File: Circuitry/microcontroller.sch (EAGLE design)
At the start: 8 parts

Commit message: fix the microcontroller board
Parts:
- removed SPACER: (no value), pinhead:PINHD-1X10
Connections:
- net N$1: now also TRANSISTOR.3; no longer LED.1
- net N$2: now also LED.1; no longer TRANSISTOR.3
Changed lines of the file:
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@@
 <part name="ESP1-15" library="pinhead" library_urn="urn:adsk.eagle:library:325" deviceset="PINHD-1X15" device="" package3d_urn="urn:adsk.eagle:package:22424/2"/>
 <part name="ESP16-30" library="pinhead" library_urn="urn:adsk.eagle:library:325" deviceset="PINHD-1X15" device="" package3d_urn="urn:adsk.eagle:package:22424/2"/>
-<part name="SPACER" library="pinhead" library_urn="urn:adsk.eagle:library:325" deviceset="PINHD-1X10" device="" package3d_urn="urn:adsk.eagle:package:22406/2"/>
 <part name="R1" library="rcl" library_urn="urn:adsk.eagle:library:334" deviceset="R-US_" device="0207/7" package3d_urn="urn:adsk.eagle:package:23493/2"/>
 </parts>
@@
 <attribute name="VALUE" x="33.02" y="44.45" size="1.778" layer="96" rot="R270"/>
 </instance>
-<instance part="SPACER" gate="A" x="106.68" y="60.96" smashed="yes">
-<attribute name="NAME" x="100.33" y="74.295" size="1.778" layer="95"/>
-<attribute name="VALUE" x="100.33" y="43.18" size="1.778" layer="96"/>
-</instance>
 <instance part="R1" gate="G$1" x="55.88" y="60.96" smashed="yes" rot="R90">
 <attribute name="NAME" x="54.3814" y="57.15" size="1.778" layer="95" rot="R90"/>
@@
 <net name="N$1" class="0">
 <segment>
-<pinref part="LED" gate="G$1" pin="1"/>
-<wire x1="12.7" y1="60.96" x2="12.7" y2="83.82" width="0.1524" layer="91"/>
-<wire x1="12.7" y1="83.82" x2="71.12" y2="83.82" width="0.1524" layer="91"/>
 <pinref part="SWITCH" gate="G$1" pin="1"/>
 <wire x1="71.12" y1="83.82" x2="78.74" y2="83.82" width="0.1524" layer="91"/>
@@
 <pinref part="ESP1-15" gate="A" pin="14"/>
 <wire x1="71.12" y1="71.12" x2="71.12" y2="83.82" width="0.1524" layer="91"/>
-<junction x="71.12" y="83.82"/>
+<pinref part="TRANSISTOR" gate="A" pin="3"/>
+<wire x1="58.42" y1="50.8" x2="58.42" y2="58.42" width="0.1524" layer="91"/>
+<wire x1="58.42" y1="58.42" x2="71.12" y2="58.42" width="0.1524" layer="91"/>
+<wire x1="71.12" y1="58.42" x2="71.12" y2="71.12" width="0.1524" layer="91"/>
+<junction x="71.12" y="71.12"/>
 </segment>
 </net>
@@
 <segment>
 <pinref part="ESP1-15" gate="A" pin="15"/>
-<wire x1="73.66" y1="71.12" x2="73.66" y2="60.96" width="0.1524" layer="91"/>
-<pinref part="TRANSISTOR" gate="A" pin="3"/>
-<wire x1="73.66" y1="60.96" x2="58.42" y2="60.96" width="0.1524" layer="91"/>
-<wire x1="58.42" y1="60.96" x2="58.42" y2="50.8" width="0.1524" layer="91"/>
 <pinref part="BOOSTCONVERTER" gate="G$1" pin="2"/>
-<wire x1="73.66" y1="60.96" x2="73.66" y2="48.26" width="0.1524" layer="91"/>
+<wire x1="73.66" y1="71.12" x2="73.66" y2="48.26" width="0.1524" layer="91"/>
 <wire x1="73.66" y1="48.26" x2="86.36" y2="48.26" width="0.1524" layer="91"/>
-<junction x="73.66" y="60.96"/>
+<pinref part="LED" gate="G$1" pin="1"/>
+<wire x1="12.7" y1="60.96" x2="12.7" y2="78.74" width="0.1524" layer="91"/>
+<wire x1="12.7" y1="78.74" x2="73.66" y2="78.74" width="0.1524" layer="91"/>
+<wire x1="73.66" y1="78.74" x2="73.66" y2="71.12" width="0.1524" layer="91"/>
+<junction x="73.66" y="71.12"/>
 </segment>
 </net>

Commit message: add initial components and header pins to board
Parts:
- removed BOOSTCONVERTER, LED, SWITCH: (no value), pinhead:PINHD-1X2
- removed ESP1-15, ESP16-30: (no value), pinhead:PINHD-1X15
- removed R1: (no value), rcl:R-US_0207/7
- removed TRANSISTOR: (no value), pinhead:PINHD-1X3
- added BAT_READ, TRIGGER: (no value), pinhead:PINHD-1X1
- added IR_LED, OLED, PWR: (no value), pinhead:PINHD-1X2
- added IR_TRS: 2N5088, transistor-npn:2N5088
- added JP3, JP4: (no value), pinhead:PINHD-1X15
- added LED_CTRL: (no value), pinhead:PINHD-1X4
- added SHIFT_REG: (no value), pinhead:PINHD-1X5
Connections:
- removed net N$2: BOOSTCONVERTER.2, ESP1-15.15, LED.1
- removed net N$3: R1.1, TRANSISTOR.2
- removed net N$4: ESP16-30.14, R1.2
- removed net N$5: ESP16-30.13, SWITCH.2
- removed net N$6: LED.2, TRANSISTOR.1
- new net 0: IR_LED.2, JP3.14, LED_CTRL.4, PWR.2, SHIFT_REG.5
- new net BATTERY_CHECKER: BAT_READ.1, JP3.1
- new net B_CTRL: JP4.13, LED_CTRL.3
- new net CLOCK: JP4.8, SHIFT_REG.3
- new net DATA: JP4.5, SHIFT_REG.2
- new net G_CTRL: JP4.11, LED_CTRL.2
- new net IR_LED: IR_TRS.B, JP4.4
- new net LATCH: JP4.9, SHIFT_REG.4
- new net OLED_SCL_PIN: JP4.2, OLED.1
- new net OLED_SDA: JP4.3, OLED.2
- new net R_CTRL: JP4.10, LED_CTRL.1
- new net TRIGGER: JP4.1, TRIGGER.1
- new net VCC: IR_TRS.C, JP3.15, PWR.1, SHIFT_REG.1
- net N$1: now also IR_LED.1, IR_TRS.E; no longer BOOSTCONVERTER.1, ESP1-15.14, SWITCH.1, TRANSISTOR.3
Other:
- note added: "A0 - GPIO 16"
- note added: "ESP Top View"
- note added: "Vin ----- 3.3 V"

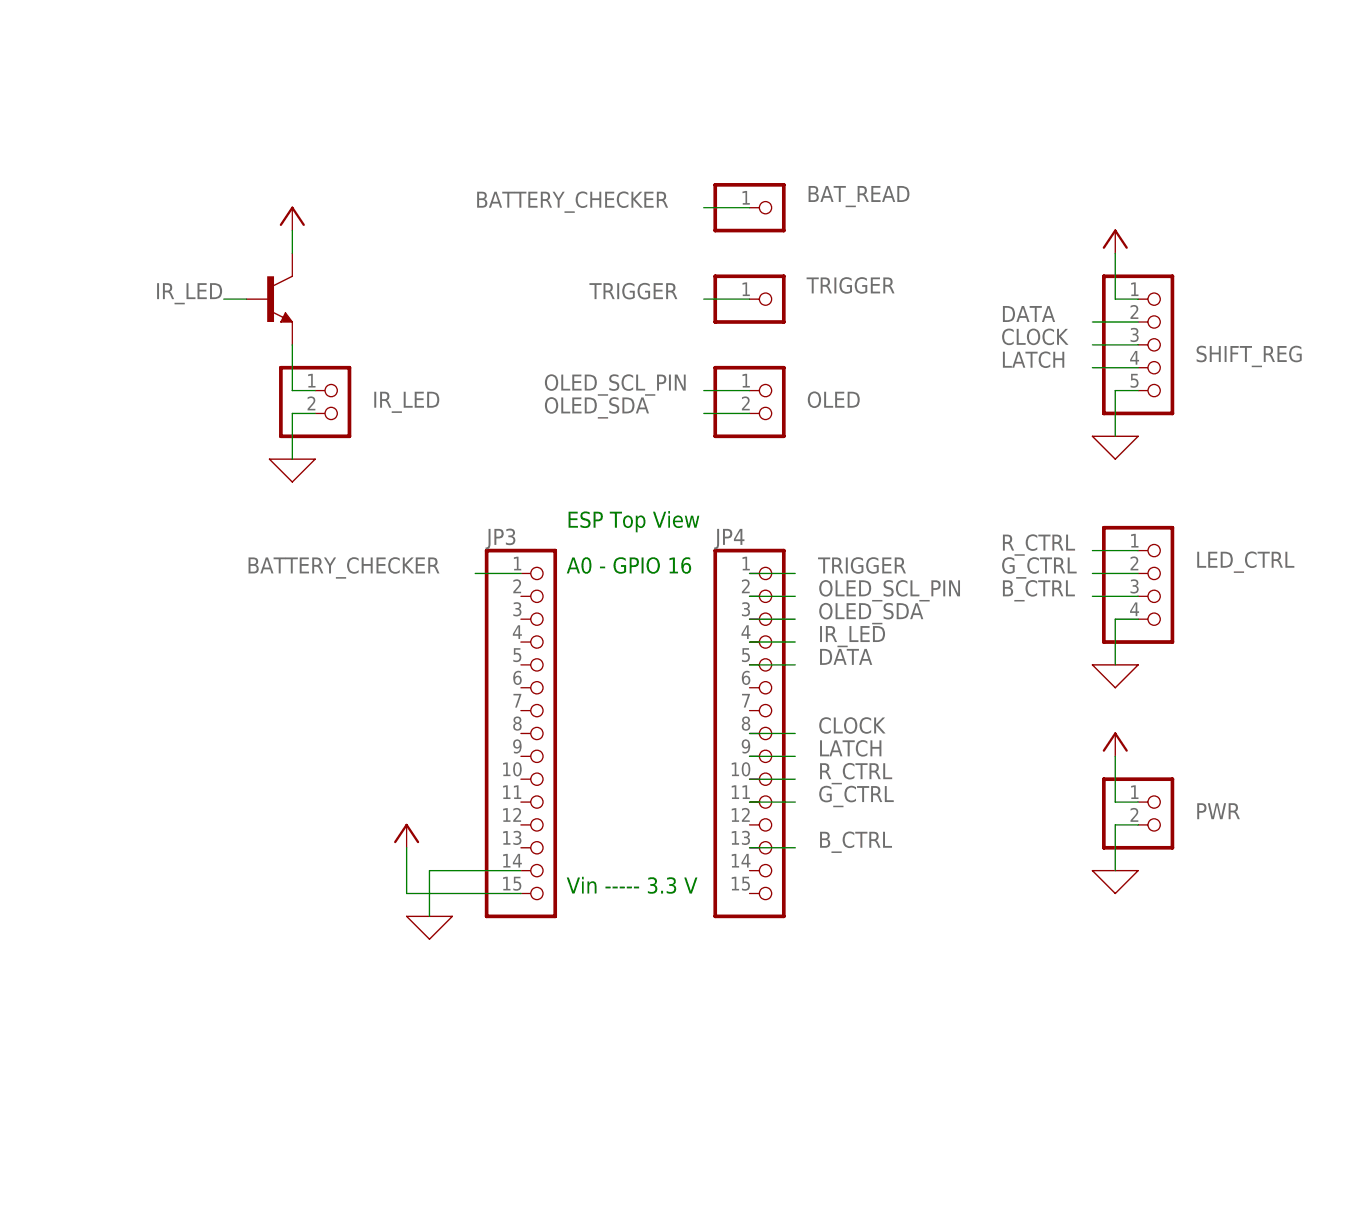
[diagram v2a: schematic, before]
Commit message: create microcontroller board
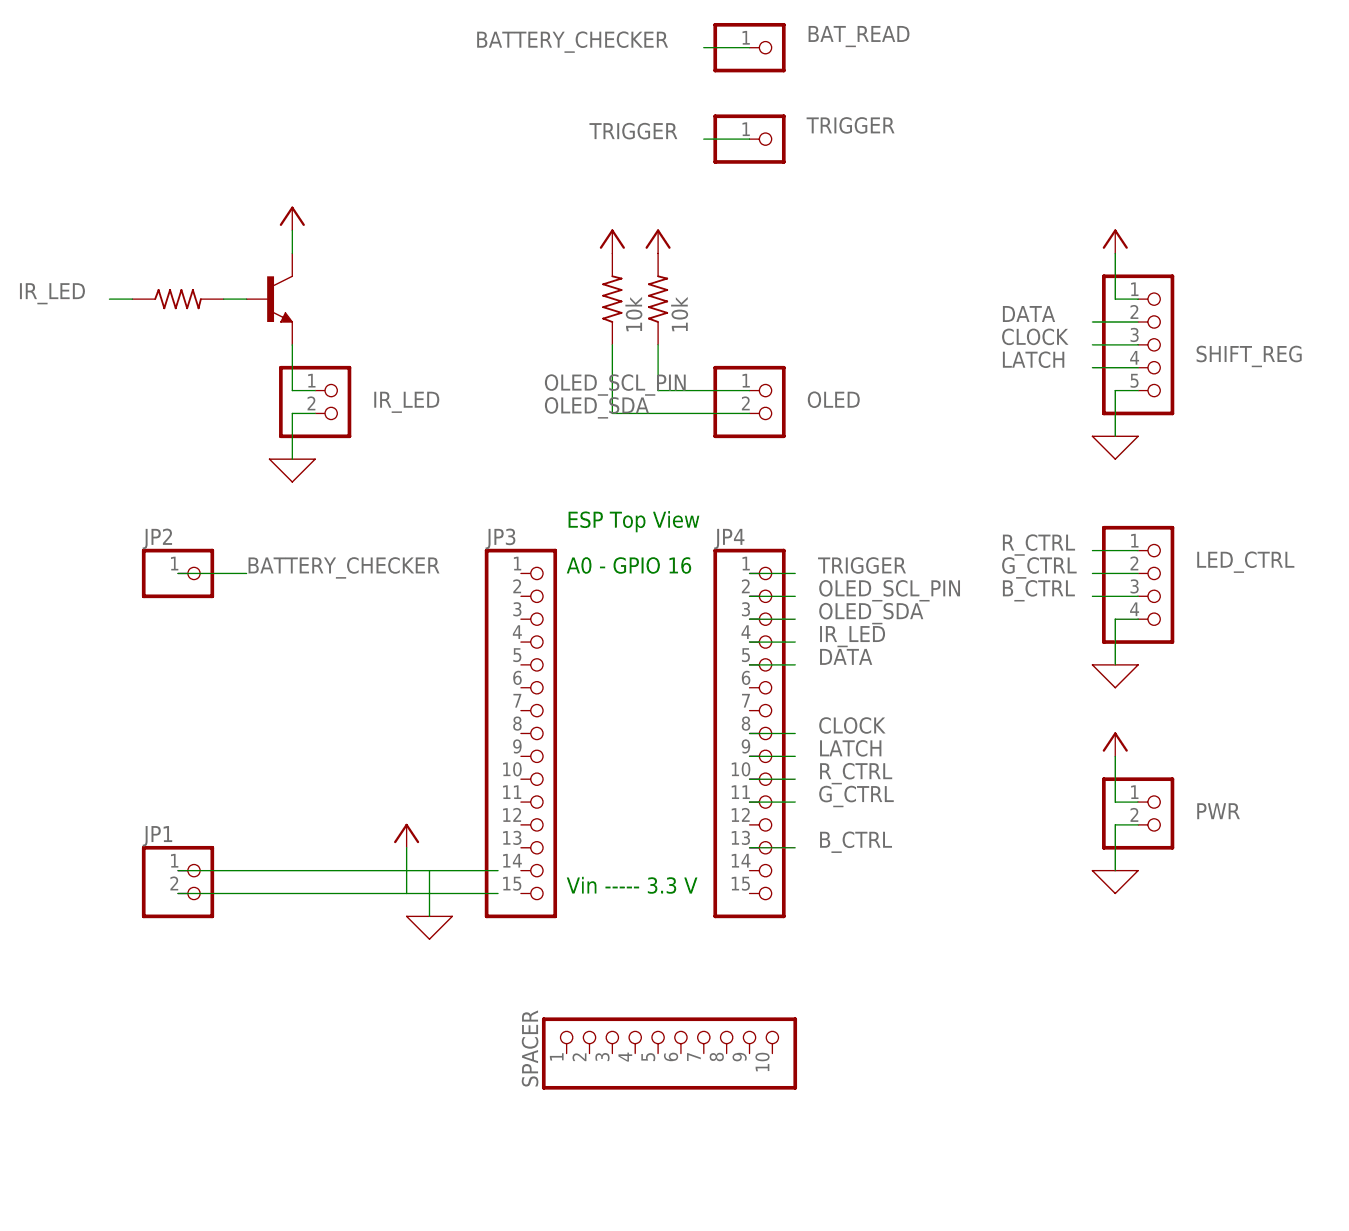
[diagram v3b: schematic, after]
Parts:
- added JP1: (no value), pinhead:PINHD-1X2
- added JP2: (no value), pinhead:PINHD-1X1
- added R1, R2: 10k, rcl:R-US_0204/7
- added R3: (no value), rcl:R-US_0204/7
- added SPACER: (no value), pinhead:PINHD-1X10
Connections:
- new net N$2: IR_TRS.B, R3.2
- net 0: now also JP1.1; no longer JP3.14
- net BATTERY_CHECKER: now also JP2.1; no longer JP3.1
- net IR_LED: now also R3.1; no longer IR_TRS.B
- net OLED_SCL_PIN: now also R1.1
- net OLED_SDA: now also R2.1
- net VCC: now also JP1.2, R1.2, R2.2; no longer JP3.15
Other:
- moved on the sheet: BAT_READ, TRIGGER

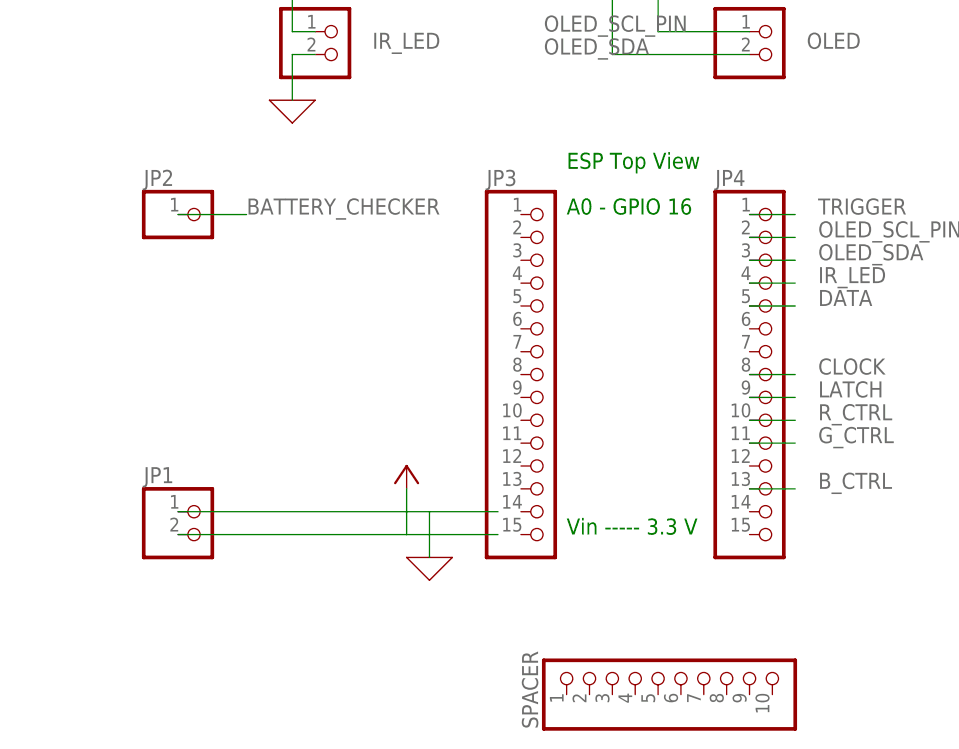
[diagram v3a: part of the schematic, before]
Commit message: remove header pins
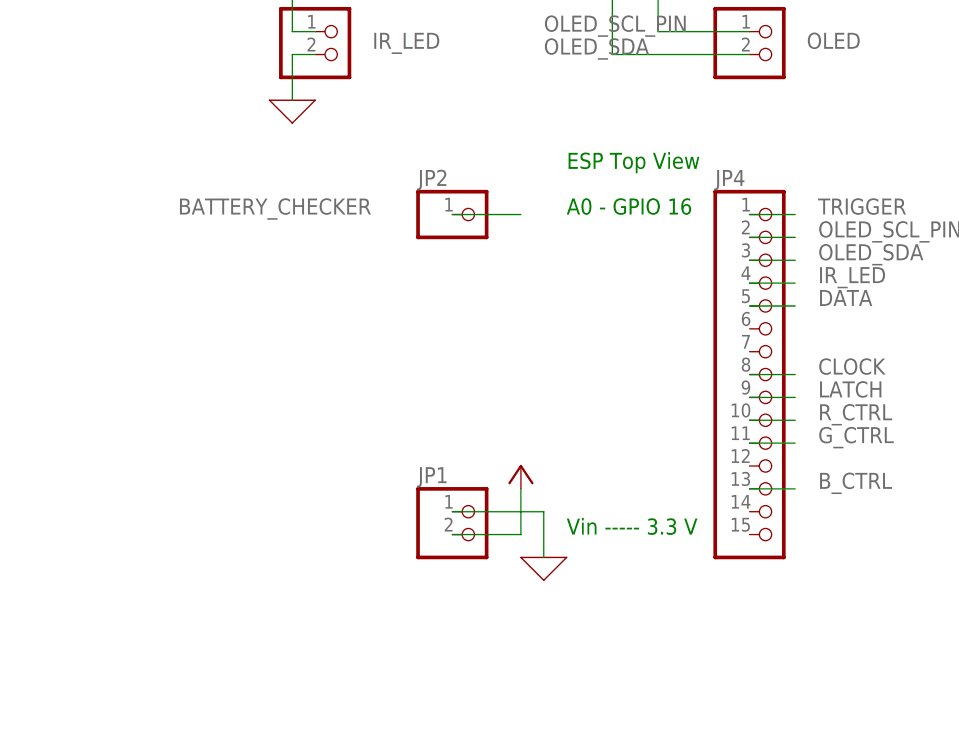
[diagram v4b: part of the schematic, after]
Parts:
- removed JP3: (no value), pinhead:PINHD-1X15
- removed SPACER: (no value), pinhead:PINHD-1X10
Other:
- moved on the sheet: JP1, JP2
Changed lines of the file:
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@@
 <part name="X_4" library="ngspice-simulation" library_urn="urn:adsk.eagle:library:527439" deviceset="GND" device=""/>
 <part name="P+3" library="supply1" library_urn="urn:adsk.eagle:library:371" deviceset="VCC" device=""/>
-<part name="JP3" library="pinhead" library_urn="urn:adsk.eagle:library:325" deviceset="PINHD-1X15" device="" package3d_urn="urn:adsk.eagle:package:22424/2"/>
 <part name="JP4" library="pinhead" library_urn="urn:adsk.eagle:library:325" deviceset="PINHD-1X15" device="" package3d_urn="urn:adsk.eagle:package:22424/2"/>
 <part name="X_5" library="ngspice-simulation" library_urn="urn:adsk.eagle:library:527439" deviceset="GND" device=""/>
 <part name="P+4" library="supply1" library_urn="urn:adsk.eagle:library:371" deviceset="VCC" device=""/>
-<part name="SPACER" library="pinhead" library_urn="urn:adsk.eagle:library:325" deviceset="PINHD-1X10" device="" package3d_urn="urn:adsk.eagle:package:22406/2"/>
 <part name="JP1" library="pinhead" library_urn="urn:adsk.eagle:library:325" deviceset="PINHD-1X2" device="" package3d_urn="urn:adsk.eagle:package:22435/2"/>
 <part name="JP2" library="pinhead" library_urn="urn:adsk.eagle:library:325" deviceset="PINHD-1X1" device="" package3d_urn="urn:adsk.eagle:package:22485/2"/>
@@
 <instance part="X_4" gate="G$1" x="17.78" y="114.3" smashed="yes"/>
 <instance part="P+3" gate="VCC" x="17.78" y="142.24" smashed="yes"/>
-<instance part="JP3" gate="A" x="45.72" y="83.82" smashed="yes">
-<attribute name="NAME" x="39.37" y="104.775" size="1.778" layer="95"/>
-<attribute name="VALUE" x="39.37" y="60.96" size="1.778" layer="96"/>
-</instance>
 <instance part="JP4" gate="A" x="71.12" y="83.82" smashed="yes">
 <attribute name="NAME" x="64.77" y="104.775" size="1.778" layer="95"/>
 <attribute name="VALUE" x="64.77" y="60.96" size="1.778" layer="96"/>
 </instance>
-<instance part="X_5" gate="G$1" x="33.02" y="63.5" smashed="yes"/>
-<instance part="P+4" gate="VCC" x="30.48" y="73.66" smashed="yes"/>
-<instance part="SPACER" gate="A" x="58.42" y="50.8" smashed="yes" rot="R90">
-<attribute name="NAME" x="45.085" y="44.45" size="1.778" layer="95" rot="R90"/>
-<attribute name="VALUE" x="76.2" y="44.45" size="1.778" layer="96" rot="R90"/>
-</instance>
-<instance part="JP1" gate="G$1" x="7.62" y="66.04" smashed="yes">
-<attribute name="NAME" x="1.27" y="71.755" size="1.778" layer="95"/>
-<attribute name="VALUE" x="1.27" y="60.96" size="1.778" layer="96"/>
-</instance>
-<instance part="JP2" gate="G$1" x="7.62" y="101.6" smashed="yes">
-<attribute name="NAME" x="1.27" y="104.775" size="1.778" layer="95"/>
-<attribute name="VALUE" x="1.27" y="96.52" size="1.778" layer="96"/>
+<instance part="X_5" gate="G$1" x="45.72" y="63.5" smashed="yes"/>
+<instance part="P+4" gate="VCC" x="43.18" y="73.66" smashed="yes"/>
+<instance part="JP1" gate="G$1" x="38.1" y="66.04" smashed="yes">
+<attribute name="NAME" x="31.75" y="71.755" size="1.778" layer="95"/>
+<attribute name="VALUE" x="31.75" y="60.96" size="1.778" layer="96"/>
+</instance>
+<instance part="JP2" gate="G$1" x="38.1" y="101.6" smashed="yes">
+<attribute name="NAME" x="31.75" y="104.775" size="1.778" layer="95"/>
+<attribute name="VALUE" x="31.75" y="96.52" size="1.778" layer="96"/>
 </instance>
 <instance part="R1" gate="G$1" x="58.42" y="132.08" smashed="yes" rot="R90">
@@
 <segment>
 <pinref part="P+4" gate="VCC" pin="VCC"/>
-<wire x1="30.48" y1="71.12" x2="30.48" y2="66.04" width="0.1524" layer="91"/>
-<wire x1="30.48" y1="66.04" x2="40.64" y2="66.04" width="0.1524" layer="91"/>
+<wire x1="43.18" y1="71.12" x2="43.18" y2="66.04" width="0.1524" layer="91"/>
 <pinref part="JP1" gate="G$1" pin="2"/>
-<wire x1="30.48" y1="66.04" x2="5.08" y2="66.04" width="0.1524" layer="91"/>
+<wire x1="43.18" y1="66.04" x2="35.56" y2="66.04" width="0.1524" layer="91"/>
 </segment>
 <segment>
@@
 <segment>
 <pinref part="X_5" gate="G$1" pin="0"/>
-<wire x1="33.02" y1="63.5" x2="33.02" y2="68.58" width="0.1524" layer="91"/>
-<wire x1="33.02" y1="68.58" x2="40.64" y2="68.58" width="0.1524" layer="91"/>
+<wire x1="45.72" y1="63.5" x2="45.72" y2="68.58" width="0.1524" layer="91"/>
 <pinref part="JP1" gate="G$1" pin="1"/>
-<wire x1="33.02" y1="68.58" x2="5.08" y2="68.58" width="0.1524" layer="91"/>
+<wire x1="45.72" y1="68.58" x2="35.56" y2="68.58" width="0.1524" layer="91"/>
 </segment>
 </net>
@@
 <segment>
 <pinref part="JP2" gate="G$1" pin="1"/>
-<wire x1="5.08" y1="101.6" x2="12.7" y2="101.6" width="0.1524" layer="91"/>
-<label x="12.7" y="101.6" size="1.778" layer="95"/>
-</segment>
-</net>
+<wire x1="35.56" y1="101.6" x2="43.18" y2="101.6" width="0.1524" layer="91"/>
+<label x="5.08" y="101.6" size="1.778" layer="95"/>
+</segment>
+</net>
